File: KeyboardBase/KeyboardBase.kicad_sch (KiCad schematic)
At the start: 2 parts, among them J101 Conn_01x07, U101 74HC00

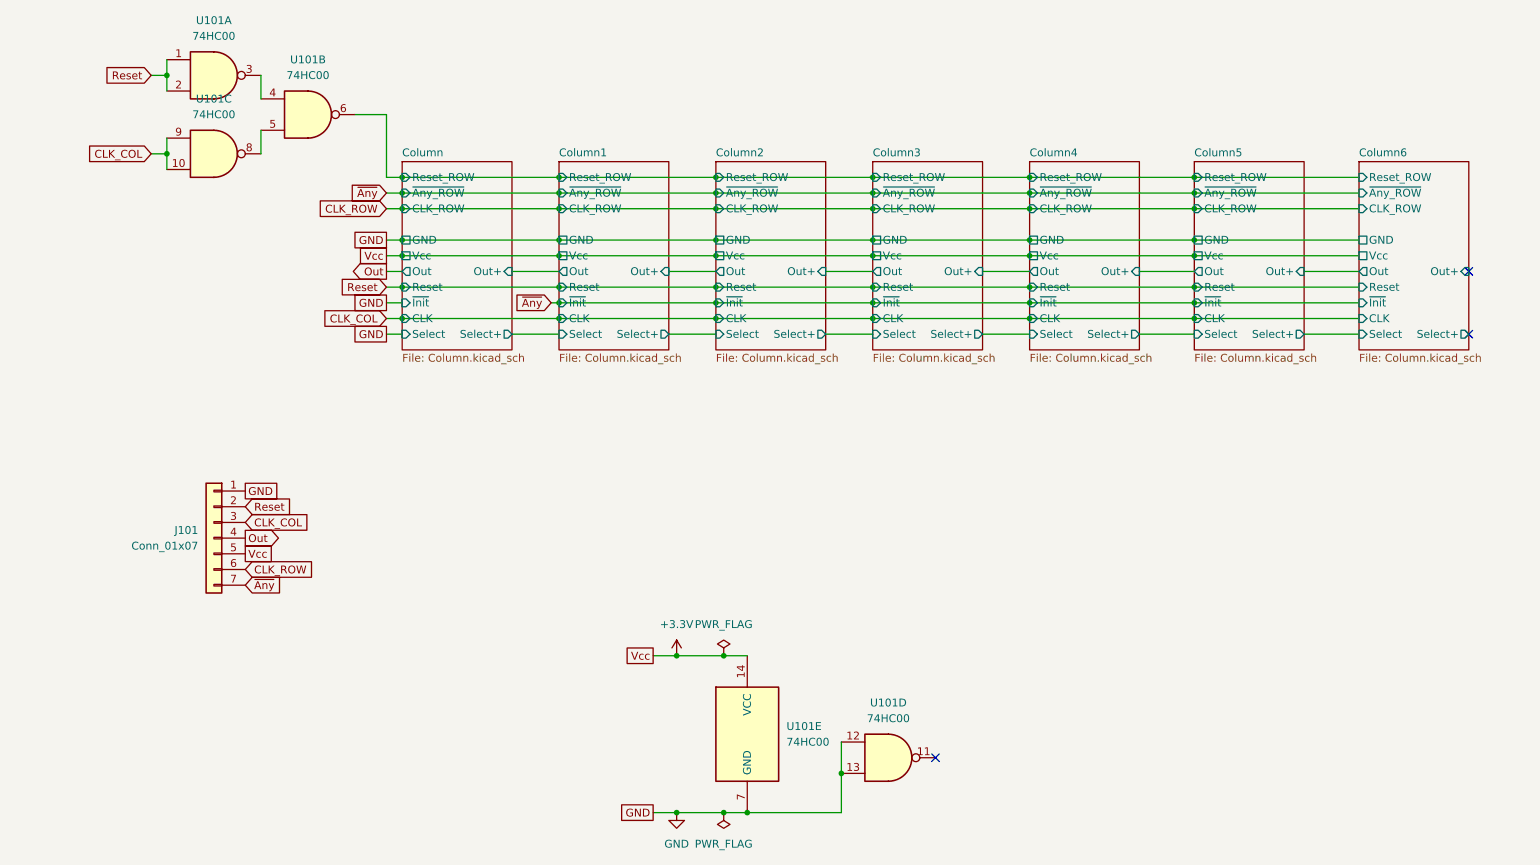
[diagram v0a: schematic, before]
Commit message: fix pin label, reduce column keys to 4
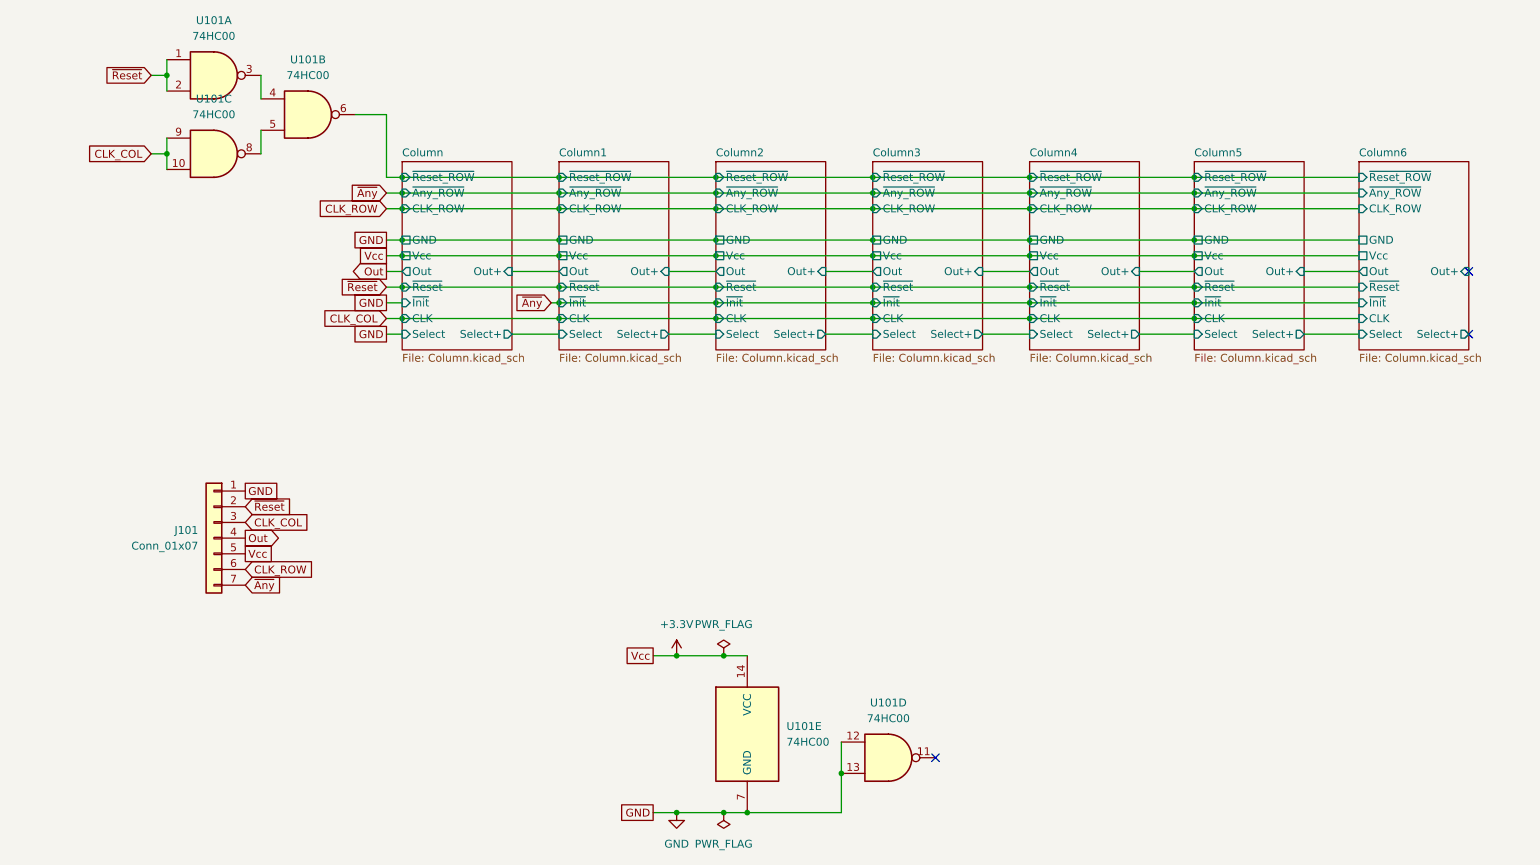
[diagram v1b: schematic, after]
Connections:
- net Column/Reset_ROW renamed Column/~{Reset_ROW}
- net Reset renamed ~{Reset}
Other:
- sheet Column ports: added ~{Reset_ROW}, ~{Reset}; removed Reset, Reset_ROW
- sheet Column1 ports: added ~{Reset_ROW}, ~{Reset}; removed Reset, Reset_ROW
- sheet Column2 ports: added ~{Reset_ROW}, ~{Reset}; removed Reset, Reset_ROW
- sheet Column3 ports: added ~{Reset_ROW}, ~{Reset}; removed Reset, Reset_ROW
- sheet Column4 ports: added ~{Reset_ROW}, ~{Reset}; removed Reset, Reset_ROW
- sheet Column5 ports: added ~{Reset_ROW}, ~{Reset}; removed Reset, Reset_ROW
- sheet Column6 ports: added ~{Reset_ROW}, ~{Reset}; removed Reset, Reset_ROW

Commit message: fix circuit
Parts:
- added U102: 74HC00, Package_DFN_QFN:WQFN-14-1EP_2.5x2.5mm_P0.5mm_EP1.45x1.45mm, symbol 74xx:74HC00
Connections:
- net +3.3V: now also J101.7 (Pin_7), U102.14 (VCC); no longer J101.5 (Pin_5)
- net CLK_COL: now also J101.5 (Pin_5), U101.1, U101.2; no longer J101.3 (Pin_3), U101.10, U101.9
- net Column/~{Reset_ROW}: now also U101.8; no longer U101.6
- net GND: now also U102.1, U102.10, U102.2, U102.7 (GND), U102.9
- net Out: now also J101.2 (Pin_2); no longer J101.4 (Pin_4)
- net ~{Any}: now also J101.3 (Pin_3), U102.5; no longer J101.7 (Pin_7)
- net ~{Reset}: now also J101.4 (Pin_4), U101.5, U102.4; no longer J101.2 (Pin_2), U101.1, U101.2
- net at U101.4: now also U101.3; no longer U101.3
- new net: U101.10, U101.6, U101.9
- new net: U102.12, U102.13, U102.6
- new net Column/~{Init}: U102.11
- no-connect marks 3 -> 5
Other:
- moved on the sheet: U101A, U101B, U101C, U101D

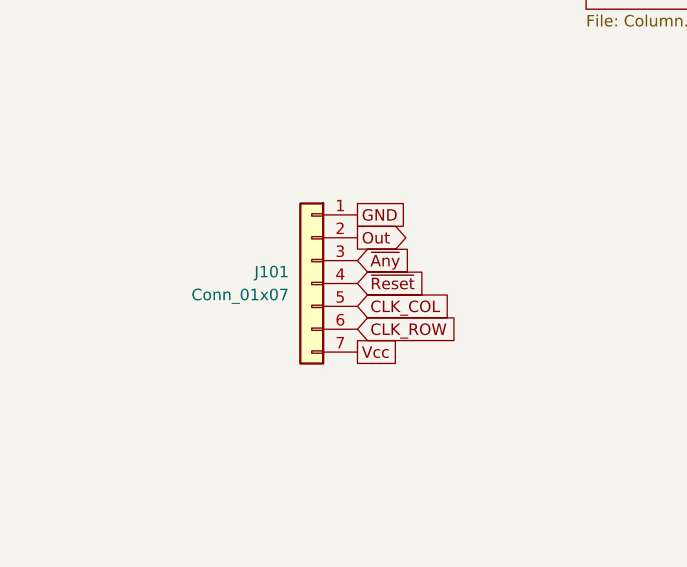
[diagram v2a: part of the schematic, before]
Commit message: change connector
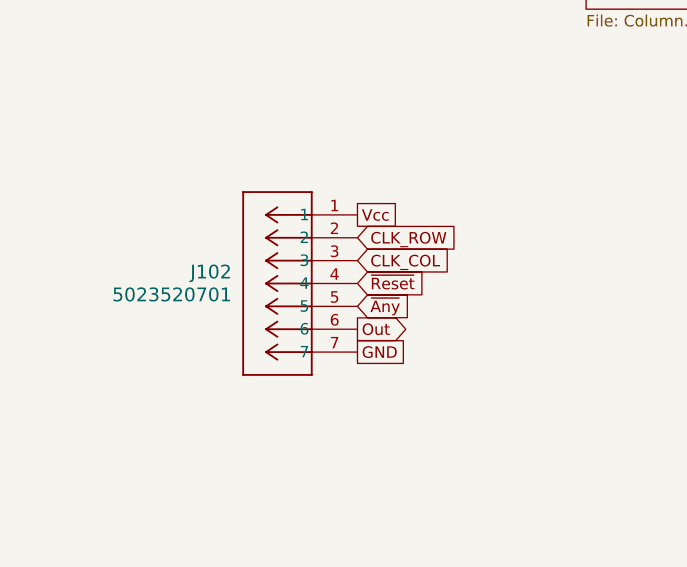
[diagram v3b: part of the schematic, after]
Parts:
- removed J101: Conn_01x07, Library:PinHeader 2.00mm 01x07 SMD, symbol Connector_Generic:Conn_01x07
- added J102: 5023520701, Molex:CONN07_502352_MOL, symbol Molex_Connector_502352:5023520701
- U101, U102: Manufacturer Part number (none) -> SN74HCS00BQAR; Original (none) -> N; Purchase Link (none) -> https://www.digikey.com/en/products/detail/texas-instrument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
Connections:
- net +3.3V: now also J102.1
- net CLK_COL: now also J102.3
- net CLK_ROW: now also J102.2
- net GND: now also J102.7
- net Out: now also J102.6
- net ~{Any}: now also J102.5
- net ~{Reset}: now also J102.4
